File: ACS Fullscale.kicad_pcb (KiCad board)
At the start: 2 copper layers, 74.9 x 74.9 mm, 35 parts, among them J1 Pulse-20, J2 Conn_01x02, U1 SN65HVD230, U10 BNO086, U11 R-78E5.0-1.0, U2 MS5611-01BA, U4 Teensy4.1, U5 TPS62202DBV, U6 BHI360, U7 TXS0108EPW, U8 BMP581, U9 BME280, Y1 32.768k

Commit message: fix lib
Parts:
- J1: footprint Sensor_Motion:Pulse-20 -> ACS_Footprint_Library:Pulse-20
- U11: footprint R-78E5.0-1.0:R-78C&slash_E-1.0_SIP3_11.6X8.5X10.4_RCP -> Converter_DCDC:Converter_DCDC_RECOM_R-78E-0.5_THT
- U4: footprint teensy:Teensy41 -> ACS_Footprint_Library:Teensy41
- U6: footprint Sensor_Motion:BHI360 Shuttle Board -> ACS_Footprint_Library:BHI360 Shuttle Board
- U8: footprint bmp581:QFN10_BMP581_BOS -> ACS_Footprint_Library:QFN10_BMP581_BOS

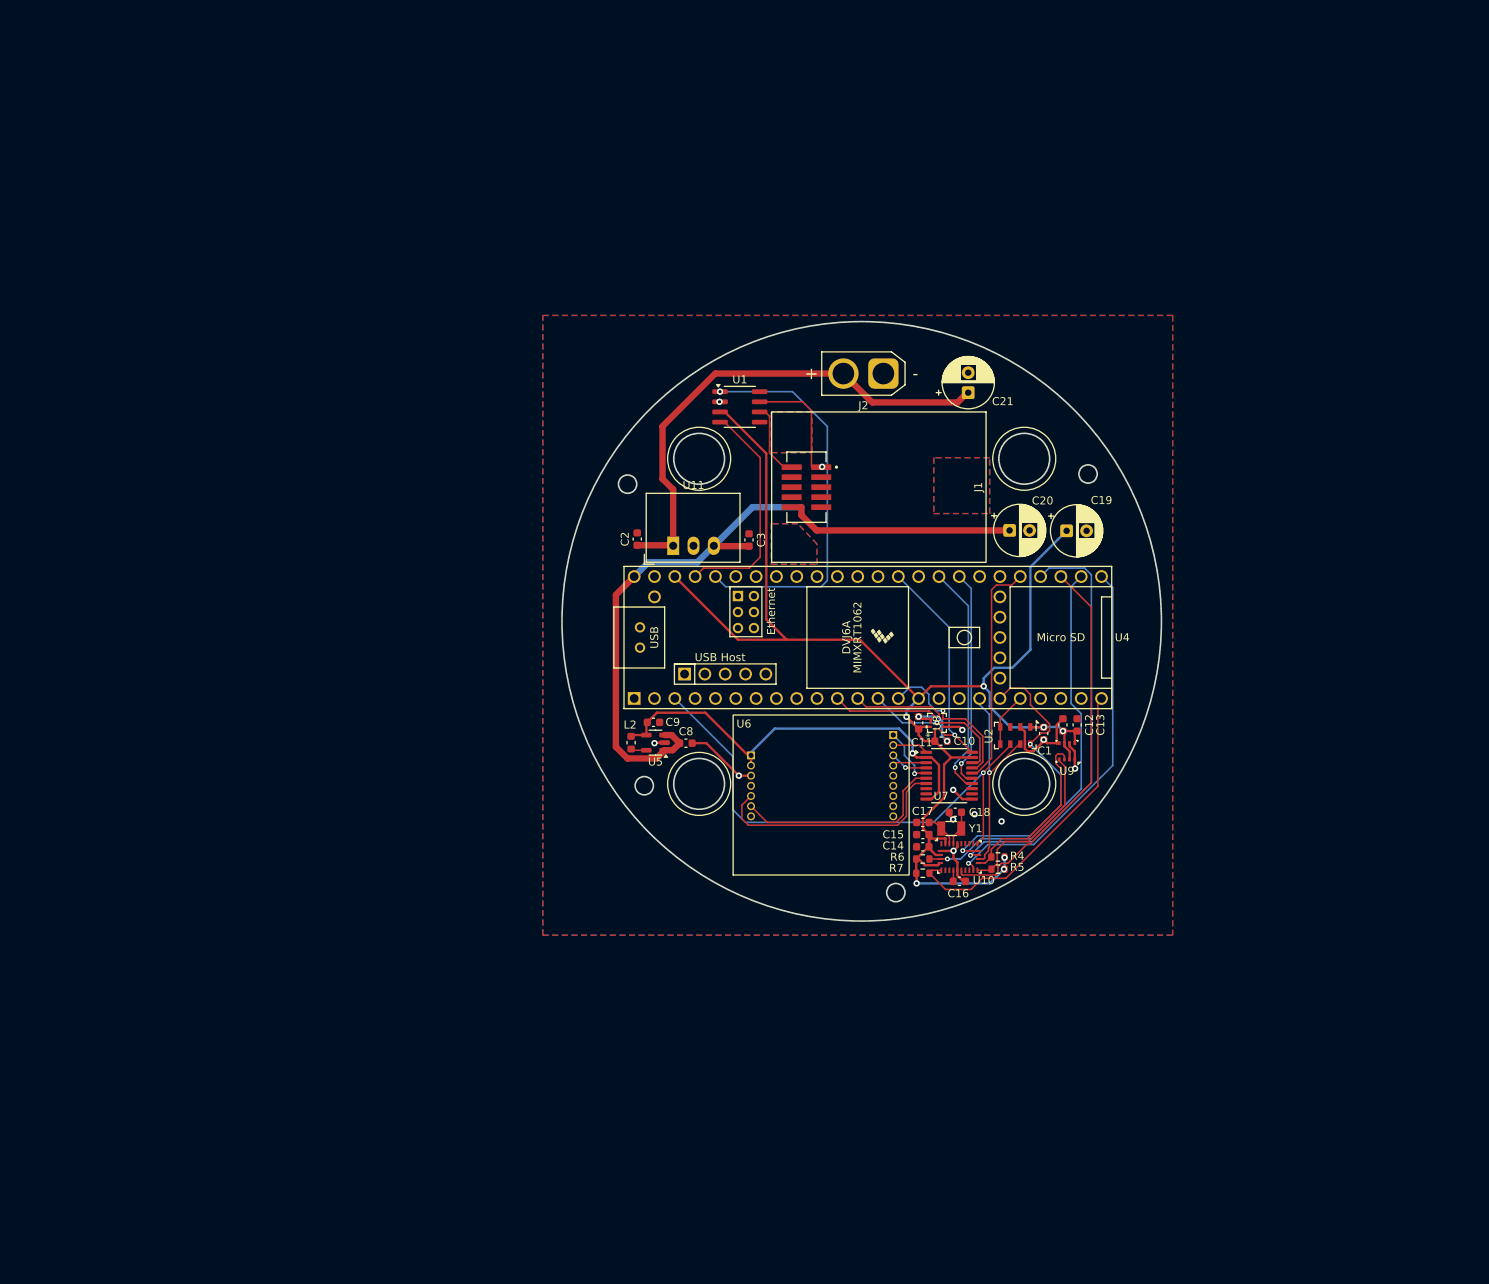
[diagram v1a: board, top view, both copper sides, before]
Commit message: I changed the diameter of the PCB to 5.95 in
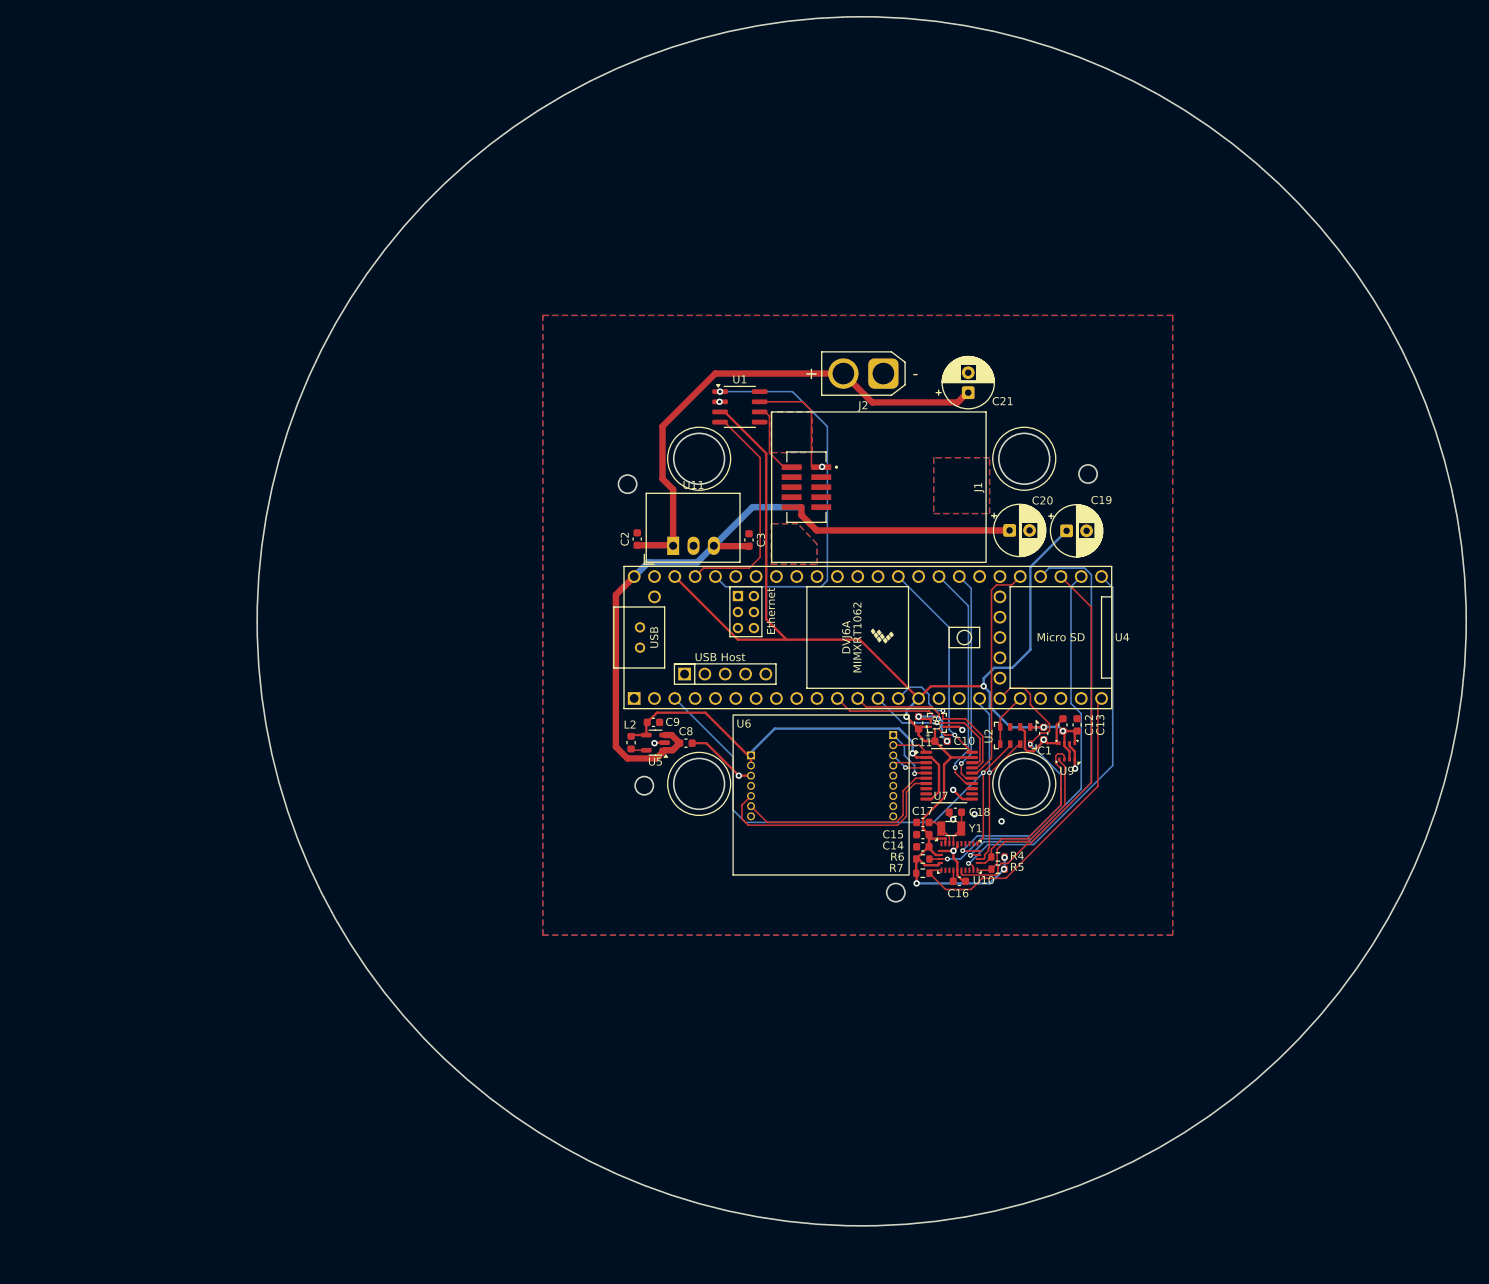
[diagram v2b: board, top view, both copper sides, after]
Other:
- board size 74.9 x 74.9 mm -> 151.1 x 151.1 mm
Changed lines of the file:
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@@
 	(gr_circle
 		(center 152.9 95.385)
-		(end 190.365 95.385)
+		(end 228.465 95.385)
 		(stroke
 			(width 0.2)

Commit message: A lot of stuff
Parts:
- added BUZZ1: CD-1206-SMT, ACS_Footprint_Library:CUI_CD-1206-SMT, F.Cu at (97.3, 69.1)
- added C6: 10u, Capacitor_SMD:C_0805_2012Metric, F.Cu at (207.5, 89.8)
- added C7: 100n, Capacitor_SMD:C_0402_1005Metric, F.Cu at (201.8, 110.9)
- added D1: LED Green, LED_SMD:LED_0603_1608Metric, F.Cu at (223.1, 100.5)
- added D2: LED Red, LED_SMD:LED_0603_1608Metric, F.Cu at (223.1, 98.7)
- added D3: D, Diode_SMD:D_SOD-323, F.Cu at (104.1, 74.2)
- added J3: Conn_02x07_Odd_Even, Connector_PinHeader_2.54mm:PinHeader_2x07_P2.54mm_Vertical, F.Cu at (188.0, 61.7)
- added J7: THD-02-R, Connector_PinHeader_2.54mm:PinHeader_2x02_P2.54mm_Vertical, F.Cu at (207.0, 124.3)
- added J8: Micro_SD_Card_Det, CM5IO:SDCARD_MOLEX_503398-1892, F.Cu at (216.8, 88.6)
- added Module1: ComputeModule5-CM5, CM5IO:Raspberry-Pi-5-Compute-Module, F.Cu at (196.6, 69.9)
- added Q1: Q_NPN_BEC, Package_TO_SOT_SMD:TSOT-23, F.Cu at (107.1, 73.6)
- added R1: 1k, Resistor_SMD:R_0402_1005Metric, F.Cu at (220.5, 100.5)
- added R10: 470R, Resistor_SMD:R_0402_1005Metric, F.Cu at (213.2, 101.3)
- added R11: 470R, Resistor_SMD:R_0402_1005Metric, F.Cu at (213.3, 102.4)
- added R12: 10K 1%, Resistor_SMD:R_0402_1005Metric, F.Cu at (207.5, 95.6)
- added R9: 1k, Resistor_SMD:R_0402_1005Metric, F.Cu at (220.5, 98.7)
- added U12: TPD4EUSB30, Package_SON:USON-10_2.5x1.0mm_P0.5mm, F.Cu at (201.7, 113.3)
- added U13: RT9742GGJ5, Package_TO_SOT_SMD:SOT-23-5, F.Cu at (207.5, 93.0)
- added U14: MagJack-A70-112-331N126, CM5IO:TRJG0926HENL, F.Cu at (213.6, 111.4)
- added U3: TPD4EUSB30, Package_SON:USON-10_2.5x1.0mm_P0.5mm, F.Cu at (201.7, 106.9)
- moved C20 87.6 mm to (83.9, 88.4)
- moved C19 80.5 mm to (98.1, 88.4)
- moved C21 78.2 mm to (91.1, 88.3), turned to 0 degrees
- moved J2 71.3 mm to (86.0, 80.1), turned to 0 degrees
- moved C11 66.3 mm to (141.4, 171.7), turned to 180 degrees
- moved U8 64.8 mm to (141.4, 169.4), turned to 180 degrees
- moved C10 63.1 mm to (143.6, 170.4), turned to -90 degrees
- moved C12 61.4 mm to (160.0, 167.0)
- moved C13 61.4 mm to (161.8, 167.0)
- moved U9 61.3 mm to (160.5, 170.2)
- moved C3 60.4 mm to (79.6, 96.9), turned to -90 degrees
- moved C1 56.0 mm to (160.4, 163.3)
- moved U2 56.0 mm to (156.8, 163.6)
- moved U7 51.4 mm to (114.2, 127.9), turned to 90 degrees
- moved R7 45.4 mm to (149.6, 170.9)
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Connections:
- U4 pad 10: unconnected-(U4-8_TX2_IN1-Pad10) -> /TX2
- U4 pad 11: /INT0 -> /CS0
- U4 pad 12: /CS0 -> unconnected-(U4-10_CS_MQSR-Pad12)
- U4 pad 16: unconnected-(U4-24_A10_TX6_SCL2-Pad16) -> /INT2
- U4 pad 17: unconnected-(U4-25_A11_RX6_SDA2-Pad17) -> /RST2
- U4 pad 20: /CS1 -> /BT3
- U4 pad 21: unconnected-(U4-29_TX7-Pad21) -> /WAKE3
- U4 pad 22: unconnected-(U4-30_CRX3-Pad22) -> /RST3
- U4 pad 23: unconnected-(U4-31_CTX3-Pad23) -> /INT3
- U4 pad 24: /WAKE3 -> /CS3
- U4 pad 25: /INT3 -> unconnected-(U4-33_MCLK2-Pad25)
- U4 pad 26: /BT3 -> unconnected-(U4-34_RX8-Pad26)
- U4 pad 27: /RST3 -> unconnected-(U4-35_TX8-Pad27)
- U4 pad 28: /CS3 -> unconnected-(U4-36_CS-Pad28)
- U4 pad 29: /CS2 -> unconnected-(U4-37_CS-Pad29)
- U4 pad 32: /INT2 -> /CS1
- U4 pad 33: /RST2 -> /CS2
- U4 pad 39: unconnected-(U4-17_A3_TX4_SDA1-Pad39) -> /Buzz
- U4 pad 8: unconnected-(U4-6_OUT1D-Pad8) -> /INT0
- U4 pad 9: unconnected-(U4-7_RX2_OUT1A-Pad9) -> /RX2
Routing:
- net /RX2: track 0.00 -> 111.9 mm, vias 0 -> 1
- net +3V3: track 182.6 -> 293.8 mm, vias 7 -> 6
- net /TX2: track 0.00 -> 109.5 mm, vias 0 -> 1
- net /CS1: track 6.74 -> 72.7 mm
- net /INT0: track 13.1 -> 68.7 mm
- net /CS0: track 11.3 -> 64.9 mm
- net /SCK0: track 28.1 -> 81.0 mm, vias 1 -> 2
- net +5V: track 91.0 -> 143.4 mm, vias 0 -> 1
- net /MISO0: track 19.8 -> 66.4 mm, vias 1 -> 0
- net +BATT: track 63.0 -> 16.9 mm
- net /MOSI1: track 26.9 -> 71.7 mm, vias 1 -> 0
- net /MOSI0: track 18.7 -> 61.6 mm, vias 1 -> 2
- net /CM5_GPIO ( Ethernet, GPIO, SDCARD)/USBOTG: track 0.00 -> 42.7 mm
- net /CM5_GPIO ( Ethernet, GPIO, SDCARD)/SYNC_OUT: track 0.00 -> 39.3 mm
- net /MISO1: track 65.6 -> 104.5 mm, vias 1 -> 2
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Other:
- board size 151.1 x 151.1 mm -> 151 x 151 mm

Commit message: ryan
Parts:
- added J4: Conn_01x03, Connector_PinHeader_2.54mm:PinHeader_1x03_P2.54mm_Vertical, F.Cu at (102.4, 79.2)
- added J5: Conn_01x03, Connector_PinHeader_2.54mm:PinHeader_1x03_P2.54mm_Vertical, F.Cu at (102.4, 83.1)
- added J6: Conn_01x05, Connector_PinHeader_2.54mm:PinHeader_1x05_P2.54mm_Vertical, F.Cu at (181.6, 125.2)
- added J9: Conn_01x02, Connector_PinHeader_2.54mm:PinHeader_1x02_P2.54mm_Vertical, F.Cu at (203.2, 78.5)
- added R2: 120, LED_SMD:LED_0603_1608Metric, F.Cu at (115.2, 88.3)
- added R3: 120, LED_SMD:LED_0603_1608Metric, F.Cu at (114.4, 95.5)
- moved J1 6.71 mm to (120.6, 85.0)
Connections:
- Module1 pad 28: /CM5_GPIO ( Ethernet, GPIO, SDCARD)/GPIO13 -> /PWM2
- Module1 pad 31: /CM5_GPIO ( Ethernet, GPIO, SDCARD)/GPIO12 -> /PWM1
- Module1 pad 77: /+5v -> +5V
- Module1 pad 79: /+5v -> +5V
- Module1 pad 81: /+5v -> +5V
- Module1 pad 83: /+5v -> +5V
- Module1 pad 85: /+5v -> +5V
- Module1 pad 87: /+5v -> +5V
- U4 pad 28: unconnected-(U4-36_CS-Pad28) -> /PWM2
- U4 pad 29: unconnected-(U4-37_CS-Pad29) -> /PWM1
- U4 pad 40: unconnected-(U4-18_A4_SDA-Pad40) -> /Motor1
- U4 pad 41: unconnected-(U4-19_A5_SCL-Pad41) -> /Motor2
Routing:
- net GND: track 33.9 -> 161.3 mm, vias 2 -> 18
- net +5V: track 143.4 -> 256.3 mm, vias 1 -> 3
- net +3V3: track 293.8 -> 368.6 mm, vias 6 -> 7
- net /PWM1: track 0.00 -> 70.3 mm, vias 0 -> 2
- net /PWM2: track 0.00 -> 64.8 mm, vias 0 -> 2
- net /CM5_GPIO ( Ethernet, GPIO, SDCARD)/GPIO10: track 0.00 -> 39.5 mm, vias 0 -> 1
- net /CM5_GPIO ( Ethernet, GPIO, SDCARD)/GPIO9: track 0.00 -> 37.5 mm, vias 0 -> 1
- net /CM5_GPIO ( Ethernet, GPIO, SDCARD)/GPIO11: track 0.00 -> 37.0 mm, vias 0 -> 1
- net /CM5_GPIO ( Ethernet, GPIO, SDCARD)/GPIO7: track 0.00 -> 36.3 mm, vias 0 -> 1
- net /CM5_GPIO ( Ethernet, GPIO, SDCARD)/GPIO8: track 0.00 -> 35.8 mm, vias 0 -> 1
- net /Motor1: track 0.00 -> 26.1 mm
- net /CM5_GPIO ( Ethernet, GPIO, SDCARD)/GPIO3: track 0.00 -> 23.0 mm, vias 0 -> 1
- net /Motor2: track 0.00 -> 21.7 mm
- net /CANH: track 9.72 -> 27.6 mm
- net /CM5_GPIO ( Ethernet, GPIO, SDCARD)/GPIO2: track 0.00 -> 17.2 mm, vias 0 -> 1
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
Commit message: lots
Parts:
- removed C10, C11, C12, C13, C14, C15, C16: 100nF, Capacitor_SMD:C_0603_1608Metric
- removed C17, C18: 22pF, Capacitor_SMD:C_0603_1608Metric
- removed C19, C21: 100uF, Capacitor_THT:CP_Radial_D6.3mm_P2.50mm
- removed C6: 10u, Capacitor_SMD:C_0805_2012Metric
- removed C7: 100n, Capacitor_SMD:C_0402_1005Metric
- removed C8: 4.7uF, Capacitor_SMD:C_0603_1608Metric
- removed C9: 10uF, Capacitor_SMD:C_0603_1608Metric
- removed D1: LED Green, LED_SMD:LED_0603_1608Metric
- removed D2: LED Red, LED_SMD:LED_0603_1608Metric
- removed J3: Conn_02x07_Odd_Even, Connector_PinHeader_2.54mm:PinHeader_2x07_P2.54mm_Vertical
- removed J6: Conn_01x05, Connector_PinHeader_2.54mm:PinHeader_1x05_P2.54mm_Vertical
- removed J7: THD-02-R, Connector_PinHeader_2.54mm:PinHeader_2x02_P2.54mm_Vertical
- removed J8: Micro_SD_Card_Det, CM5IO:SDCARD_MOLEX_503398-1892
- removed J9: Conn_01x02, Connector_PinHeader_2.54mm:PinHeader_1x02_P2.54mm_Vertical
- removed L2: 10uH, Inductor_SMD:L_0603_1608Metric
- removed Module1: ComputeModule5-CM5, CM5IO:Raspberry-Pi-5-Compute-Module
- removed R10, R11: 470R, Resistor_SMD:R_0402_1005Metric
- removed R12: 10K 1%, Resistor_SMD:R_0402_1005Metric
- removed R2, R3: 120, LED_SMD:LED_0603_1608Metric
- removed R4, R5: 4.7k, Resistor_SMD:R_0603_1608Metric
- removed R6, R7: 10k, Resistor_SMD:R_0603_1608Metric
- removed R9: 1k, Resistor_SMD:R_0402_1005Metric
- removed U1: SN65HVD230, Package_SO:SOIC-8_3.9x4.9mm_P1.27mm
- removed U10: BNO086, Package_LGA:LGA-28_5.2x3.8mm_P0.5mm
- removed U12: TPD4EUSB30, Package_SON:USON-10_2.5x1.0mm_P0.5mm
- removed U13: RT9742GGJ5, Package_TO_SOT_SMD:SOT-23-5
- removed U14: MagJack-A70-112-331N126, CM5IO:TRJG0926HENL
- removed U8: BMP581, ACS_Footprint_Library:QFN10_BMP581_BOS
- removed Y1: 32.768k, Crystal:Crystal_SMD_3215-2Pin_3.2x1.5mm
- added C4: 100uF, Capacitor_SMD:C_1206_3216Metric, F.Cu at (105.9, 61.0)
- added JP1: BNO_DI, Jumper:SolderJumper-3_P1.3mm_Bridged2Bar12_RoundedPad1.0x1.5mm, B.Cu at (76.6, 103.1)
- added JP10: LSM_SDOAG, Jumper:SolderJumper-3_P1.3mm_Bridged2Bar12_RoundedPad1.0x1.5mm, B.Cu at (97.0, 72.5)
- added JP11: LSM_SDOM, Jumper:SolderJumper-3_P1.3mm_Bridged2Bar12_RoundedPad1.0x1.5mm, B.Cu at (101.6, 72.5)
- added JP12: BNO_MOSI, Jumper:SolderJumper-3_P1.3mm_Bridged2Bar12_RoundedPad1.0x1.5mm, B.Cu at (90.0, 92.1)
- added JP13: BNO_SCK, Jumper:SolderJumper-3_P1.3mm_Bridged2Bar12_RoundedPad1.0x1.5mm, B.Cu at (92.4, 82.6)
- added JP14: BNO_MISO, Jumper:SolderJumper-3_P1.3mm_Bridged2Bar12_RoundedPad1.0x1.5mm, B.Cu at (95.1, 92.1)
- added JP15: LSM_SCK, Jumper:SolderJumper-3_P1.3mm_Bridged2Bar12_RoundedPad1.0x1.5mm, B.Cu at (107.8, 89.3)
- added JP16: LSM_MOSI, Jumper:SolderJumper-3_P1.3mm_Bridged2Bar12_RoundedPad1.0x1.5mm, B.Cu at (102.7, 89.3)
- added JP17: LSMAG_MISO, Jumper:SolderJumper-3_P1.3mm_Bridged2Bar12_RoundedPad1.0x1.5mm, B.Cu at (67.2, 92.4)
- added JP18: ICM_SCL, Jumper:SolderJumper-3_P1.3mm_Bridged2Bar12_RoundedPad1.0x1.5mm, B.Cu at (97.3, 102.1)
- added JP19: LSMAG_MISO, Jumper:SolderJumper-3_P1.3mm_Bridged2Bar12_RoundedPad1.0x1.5mm, B.Cu at (67.2, 89.5)
- added JP2: BNO_SCL, Jumper:SolderJumper-3_P1.3mm_Bridged2Bar12_RoundedPad1.0x1.5mm, B.Cu at (72.4, 114.6)
- added JP20: LSMM_MISO, Jumper:SolderJumper-3_P1.3mm_Bridged2Bar12_RoundedPad1.0x1.5mm, B.Cu at (67.2, 86.7)
- added JP21: ICM_SDA, Jumper:SolderJumper-3_P1.3mm_Bridged2Bar12_RoundedPad1.0x1.5mm, B.Cu at (92.4, 102.1)
- added JP22: ICM_SDO, Jumper:SolderJumper-3_P1.3mm_Bridged2Bar12_RoundedPad1.0x1.5mm, F.Cu at (87.6, 116.7)
- added JP3: BNO_SDA, Jumper:SolderJumper-3_P1.3mm_Bridged2Bar12_RoundedPad1.0x1.5mm, B.Cu at (77.1, 114.6)
- added JP4: BNO_P0, Jumper:SolderJumper-3_P1.3mm_Bridged2Bar12_RoundedPad1.0x1.5mm, B.Cu at (67.2, 103.1)
- added JP5: BNO_P1, Jumper:SolderJumper-3_P1.3mm_Bridged2Bar12_RoundedPad1.0x1.5mm, B.Cu at (71.9, 103.1)
- added JP6: LSM_SCL, Jumper:SolderJumper-3_P1.3mm_Bridged2Bar12_RoundedPad1.0x1.5mm, B.Cu at (86.8, 72.5)
- added JP7: LSM_SDA, Jumper:SolderJumper-3_P1.3mm_Bridged2Bar12_RoundedPad1.0x1.5mm, B.Cu at (91.4, 72.5)
- added JP8: LSM_SCK, Jumper:SolderJumper-3_P1.3mm_Bridged2Bar12_RoundedPad1.0x1.5mm, B.Cu at (107.8, 92.2)
- added JP9: LSM_MOSI, Jumper:SolderJumper-3_P1.3mm_Bridged2Bar12_RoundedPad1.0x1.5mm, B.Cu at (102.7, 92.1)
- C1: value 100nF -> 100uF; footprint Capacitor_SMD:C_0603_1608Metric -> Capacitor_SMD:C_1206_3216Metric
- C20: footprint Capacitor_THT:CP_Radial_D6.3mm_P2.50mm -> Capacitor_SMD:C_1206_3216Metric
- R1: value 1k -> 10k; footprint Resistor_SMD:R_0402_1005Metric -> Resistor_SMD:R_0805_2012Metric_Pad1.20x1.40mm_HandSolder; moved to B.Cu
- U2: value MS5611-01BA -> MS5611-01BA03; footprint Package_LGA:LGA-8_3x5mm_P1.25mm -> Sensor_Pressure:HiLetgo MS5611
- U3: value TPD4EUSB30 -> Adafruit_BNO086; footprint Package_SON:USON-10_2.5x1.0mm_P0.5mm -> Sensor_Motion:Adafruit BNO086
- U5: value TPS62202DBV -> BMP585; footprint Package_TO_SOT_SMD:SOT-23-5 -> Sensor_Pressure:DFRobot BMP585
- U6: value BHI360 -> ICM20948; footprint ACS_Footprint_Library:BHI360 Shuttle Board -> Sensor_Motion:Adafruit ICM20948
- U7: value TXS0108EPW -> LSM9DS1; footprint Package_SO:TSSOP-20_4.4x6.5mm_P0.65mm -> Sensor_Motion:Adafruit LSM9DS1
- U9: value BME280 -> LTC2851xS8; footprint Package_LGA:Bosch_LGA-8_2.5x2.5mm_P0.65mm_ClockwisePinNumbering -> Package_SO:SOIC-8_3.9x4.9mm_P1.27mm
- moved R1 155.6 mm to (64.9, 105.4)
- moved C1 134.7 mm to (61.7, 71.7), turned to 180 degrees
- moved U3 129.6 mm to (72.1, 108.8)
- moved U2 128.1 mm to (70.8, 68.6), turned to 90 degrees
- moved U9 90.0 mm to (124.4, 87.8), turned to 0 degrees
- moved U7 63.3 mm to (90.4, 69.2), turned to 0 degrees
- moved U5 60.1 mm to (113.0, 70.1), turned to 0 degrees
- moved U6 55.9 mm to (98.0, 105.9), turned to 180 degrees
- moved D3 52.4 mm to (87.1, 123.7), turned to 180 degrees
- moved BUZZ1 52.2 mm to (97.3, 121.3), turned to -90 degrees
- moved Q1 50.8 mm to (87.1, 120.4), turned to -90 degrees
- moved C3 49.0 mm to (124.5, 77.2), turned to 0 degrees
- moved U11 45.9 mm to (125.1, 67.8), turned to -90 degrees
- moved C2 45.5 mm to (123.8, 62.5), turned to 90 degrees
- moved C20 34.9 mm to (104.6, 116.5), turned to 180 degrees
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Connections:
- J1 pad 10: /CANL -> unconnected-(J1-CAN_L-Pad10)
- J1 pad 2: unconnected-(J1-PORT_A_Rx+-Pad2) -> /Rx+
- J1 pad 3: unconnected-(J1-PORT_A_Tx+-Pad3) -> /Tx+
- J1 pad 5: /CANH -> unconnected-(J1-CAN_H-Pad5)
- J1 pad 7: unconnected-(J1-PORT_A_RX--Pad7) -> /RX-
- J1 pad 8: unconnected-(J1-PORT_A_TX--Pad8) -> /TX-
- R1 pad 1: Net-(D1-K) -> /BNO_WAKE
- R1 pad 2: Net-(Module1A-LED_nACT) -> +3V3
- U2 pad 3: GND -> /SCK1
- U2 pad 4: /CS1 -> /MOSI1
- U2 pad 5: /CS1 -> /CS_MS
- U2 pad 7: /MOSI1 -> GND
- U3 pad 1: /CM5_GPIO ( Ethernet, GPIO, SDCARD)/TRD3_P -> +3V3
- U3 pad 10: /CM5_GPIO ( Ethernet, GPIO, SDCARD)/TRD3_P -> /BNO_RST
- U3 pad 2: /CM5_GPIO ( Ethernet, GPIO, SDCARD)/TRD3_N -> unconnected-(U3-3VO-Pad2)
- U3 pad 4: /CM5_GPIO ( Ethernet, GPIO, SDCARD)/TRD2_N -> /BNO_SCL
- U3 pad 5: /CM5_GPIO ( Ethernet, GPIO, SDCARD)/TRD2_P -> /BNO_SDA
- U3 pad 6: /CM5_GPIO ( Ethernet, GPIO, SDCARD)/TRD2_P -> /BNO_INT
- U3 pad 7: /CM5_GPIO ( Ethernet, GPIO, SDCARD)/TRD2_N -> unconnected-(U3-BT-Pad7)
- U3 pad 8: GND -> /BNO_P0
- U3 pad 9: /CM5_GPIO ( Ethernet, GPIO, SDCARD)/TRD3_N -> /BNO_P1
- U4 pad 11: /CS0 -> unconnected-(U4-9_OUT1C-Pad11)
- U4 pad 16: /INT2 -> /ICM_INT
- U4 pad 17: /RST2 -> /ICM_CS
- U4 pad 20: /BT3 -> /RX7
- U4 pad 21: /WAKE3 -> /TX7
- U4 pad 22: /RST3 -> unconnected-(U4-30_CRX3-Pad22)
- U4 pad 23: /INT3 -> unconnected-(U4-31_CTX3-Pad23)
- U4 pad 24: /CS3 -> unconnected-(U4-32_OUT1B-Pad24)
- U4 pad 25: unconnected-(U4-33_MCLK2-Pad25) -> /BMP_INT
- U4 pad 27: unconnected-(U4-35_TX8-Pad27) -> /BMP_CS
- U4 pad 28: /PWM2 -> unconnected-(U4-36_CS-Pad28)
- U4 pad 29: /PWM1 -> unconnected-(U4-37_CS-Pad29)
- U4 pad 31: unconnected-(U4-39_MISO1_OUT1A-Pad31) -> /LSM_INTM
- U4 pad 32: /CS1 -> /LSM_INT1
- U4 pad 33: /CS2 -> /LSM_INT2
- U4 pad 36: unconnected-(U4-14_A0_TX3_SPDIF_OUT-Pad36) -> /LSM_CSM
- U4 pad 37: unconnected-(U4-15_A1_RX3_SPDIF_IN-Pad37) -> /LSM_CSAG
- U4 pad 39: /Buzz -> unconnected-(U4-17_A3_TX4_SDA1-Pad39)
- U4 pad 4: unconnected-(U4-2_OUT2-Pad4) -> /BNO_INT
- U4 pad 40: /Motor1 -> /SDA
- U4 pad 41: /Motor2 -> /SCL
- U4 pad 43: unconnected-(U4-21_A7_RX5_BCLK1-Pad43) -> /CS_MS
- U4 pad 44: /CANTX -> /PWM2
- U4 pad 45: /CANRX -> /PWM1
- U4 pad 5: unconnected-(U4-3_LRCLK2-Pad5) -> /BNO_RST
- U4 pad 6: unconnected-(U4-4_BCLK2-Pad6) -> /BNO_CS
- U4 pad 8: /INT0 -> unconnected-(U4-6_OUT1D-Pad8)
- U5 pad 1: +5V -> +3V3
- U5 pad 3: +5V -> /SCK0
- U5 pad 4: +1V8 -> /MOSI0
- U5 pad 5: Net-(U5-SW) -> /BMP_CS
- U7 pad 1: /SCK_1V8 -> +3V3
- U7 pad 10: +1V8 -> unconnected-(U7-DEN-Pad10)
- U7 pad 11: GND -> /LSM_INT2
- U7 pad 12: unconnected-(U7-B8-Pad12) -> /LSM_INT1
- U7 pad 13: unconnected-(U7-B7-Pad13) -> /LSM_INTM
- U7 pad 14: /RST2 -> unconnected-(U7-DRDY-Pad14)
- U7 pad 2: +1V8 -> unconnected-(U7-3VO-Pad2)
- U7 pad 3: /MOSI_1V8 -> GND
- U7 pad 4: /MISO_1V8 -> /LSM_SCL
- U7 pad 5: /CS_1V8 -> /LSM_SDA
- U7 pad 6: /INT_1V8 -> /LSM_CSAG
- U7 pad 7: /RST_1V8 -> /LSM_CSM
- U7 pad 8: unconnected-(U7-A7-Pad8) -> /LSM_SDOAG
- U7 pad 9: unconnected-(U7-A8-Pad9) -> /LSM_SDOM
- U9 pad 1: GND -> +3V3
- U9 pad 2: +3V3 -> /RX7
- U9 pad 3: /BNO086/SDA -> /TX7
- U9 pad 4: /BNO086/SCL -> GND
- U9 pad 5: GND -> /RX-
- U9 pad 6: +3V3 -> /Rx+
- U9 pad 7: GND -> /TX-
- U9 pad 8: +3V3 -> /Tx+
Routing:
- net GND: track 161.3 -> 6.22 mm, vias 18 -> 10
- net +3V3: track 368.6 -> 247.5 mm, vias 7 -> 0
- net /RX2: track 111.9 -> 0.00 mm, vias 1 -> 0
- net /TX2: track 109.5 -> 0.00 mm, vias 1 -> 0
- net +5V: track 256.3 -> 157.9 mm, vias 3 -> 2
- net /SCL: track 0.00 -> 78.9 mm, vias 0 -> 1
- net /SDA: track 0.00 -> 77.1 mm, vias 0 -> 2
- net /CS1: track 72.7 -> 0.00 mm
- net /PWM1: track 70.3 -> 0.00 mm, vias 2 -> 0
- net /INT0: track 68.7 -> 0.00 mm
- net /CS0: track 64.9 -> 0.00 mm
- net /PWM2: track 64.8 -> 0.00 mm, vias 2 -> 0
- net /BT3: track 59.2 -> 0.00 mm, vias 1 -> 0
- net +BATT: track 33.0 -> 91.3 mm
- net /WAKE3: track 58.1 -> 0.00 mm, vias 1 -> 0
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- removed copper zone on B.Cu, net (none)
- removed copper zone on F.Cu, net (none)
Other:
- board size 151 x 151 mm -> 74.9 x 70.7 mm
